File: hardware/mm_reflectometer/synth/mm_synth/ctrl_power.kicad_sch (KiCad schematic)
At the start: 64 parts, among them J1501 Screw_Terminal_01x02, J1502 Conn_01x02_Female, Q1501 FDS6890A, U1501 LTM4622A, U1502 LTC4365DDB, U1503 LM3880MF-1AF, U1504 TLV70025_WSON6, U1505 TLV62569DRL, U1506 TLV62569DRL, U1507 TLV70018_WSON6

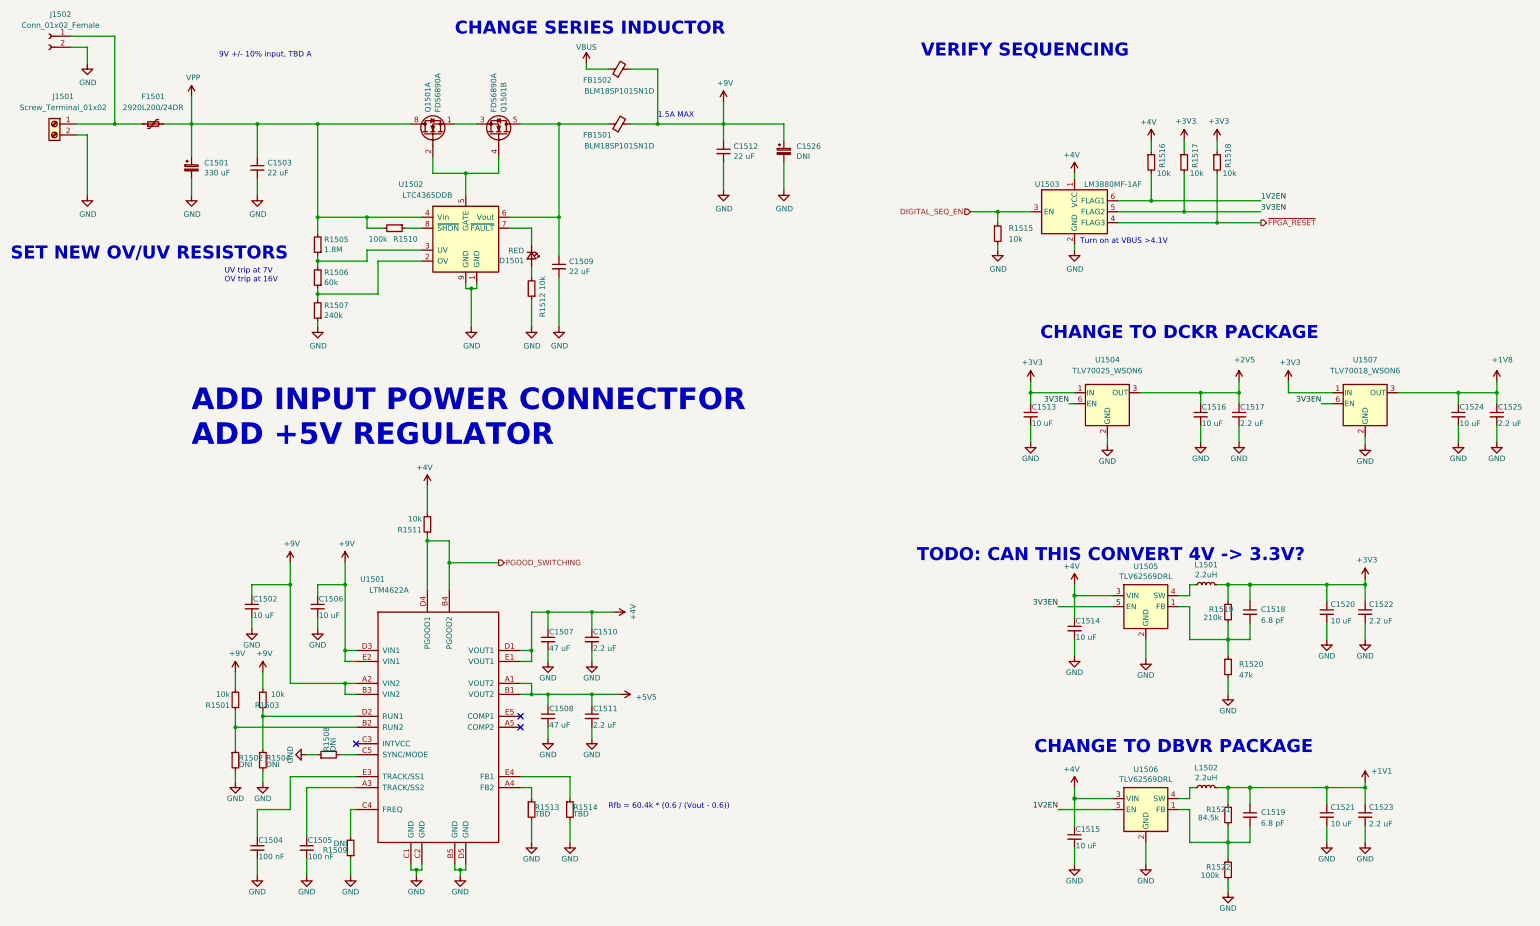
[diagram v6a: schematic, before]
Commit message: created HUSB238 eval board, added clock splitter to mm synth
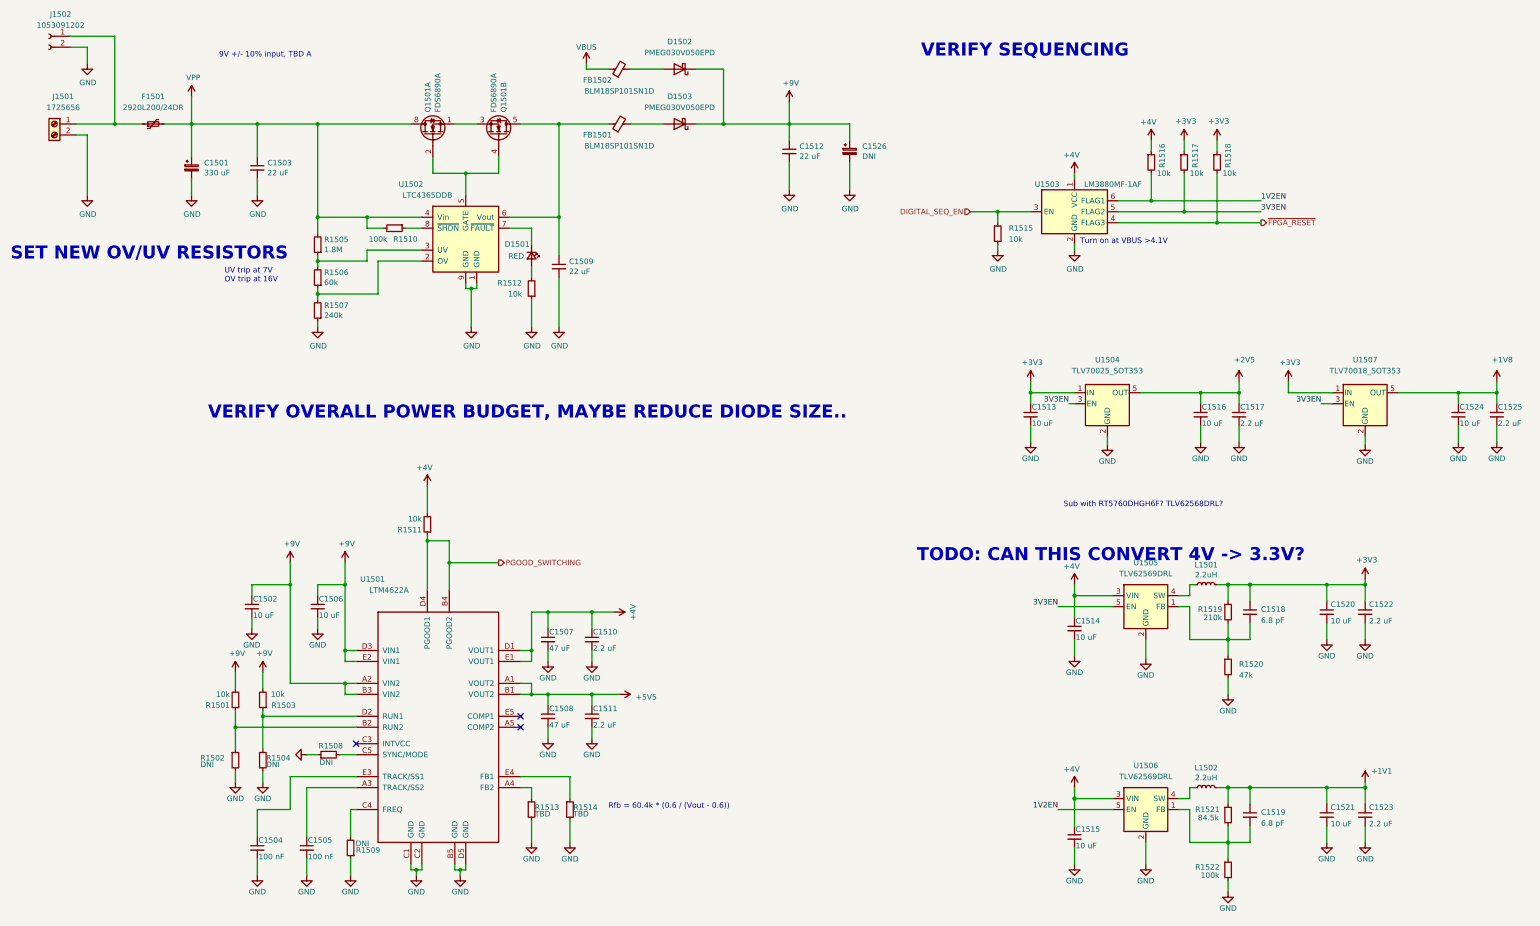
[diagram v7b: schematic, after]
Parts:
- removed U1504: TLV70025_WSON6, Package_SON:WSON-6_1.5x1.5mm_P0.5mm, symbol Regulator_Linear:TLV70025_WSON6
- removed U1507: TLV70018_WSON6, Package_SON:WSON-6_1.5x1.5mm_P0.5mm, symbol Regulator_Linear:TLV70018_WSON6
- added D1502, D1503: PMEG030V050EPD, Package_TO_SOT_SMD:Nexperia_CFP15_SOT-1289, symbol Diode:PMEG030V050EPD
- added U1504: TLV70025_SOT353, Package_TO_SOT_SMD:SOT-353_SC-70-5, symbol Regulator_Linear:TLV70025_SOT353
- added U1507: TLV70018_SOT353, Package_TO_SOT_SMD:SOT-353_SC-70-5, symbol Regulator_Linear:TLV70018_SOT353
- J1501: value Screw_Terminal_01x02 -> 1725656
- J1502: value Conn_01x02_Female -> 1053091202
- U1505, U1506: footprint Package_TO_SOT_SMD:SOT-666 -> Package_TO_SOT_SMD:SOT-563; Mfg Texas Instruments -> (none); PN TLV62569DRLR -> (none)
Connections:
- net +1V8: now also U1507.5 (OUT)
- net +2V5: now also U1504.5 (OUT)
- net +3V3: now also U1504.1 (IN), U1507.1 (IN)
- net +9V: now also D1502.3 (K), D1503.3 (K); no longer FB1501.2, FB1502.2
- net 3V3EN: now also U1504.3 (EN), U1507.3 (EN)
- net GND: now also U1504.2 (GND), U1507.2 (GND)
- new net: D1503.1 (A), D1503.2 (A), FB1501.2
- new net: D1502.1 (A), D1502.2 (A), FB1502.2
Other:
- note added: "Sub with RT5760DHGH6F? TLV62568DRL?"
- note added: "VERIFY OVERALL POWER BUDGET, MAYBE REDUCE DIODE SIZE.."
- note removed: "1.5A MAX"
- note removed: "ADD INPUT POWER CONNECTFOR ADD +5V REGULATOR"
- note removed: "CHANGE SERIES INDUCTOR"
- note removed: "CHANGE TO DBVR PACKAGE"
- note removed: "CHANGE TO DCKR PACKAGE"
- moved on the sheet: C1512, C1526

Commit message: reviewed capacitors for voltage rating and availability..
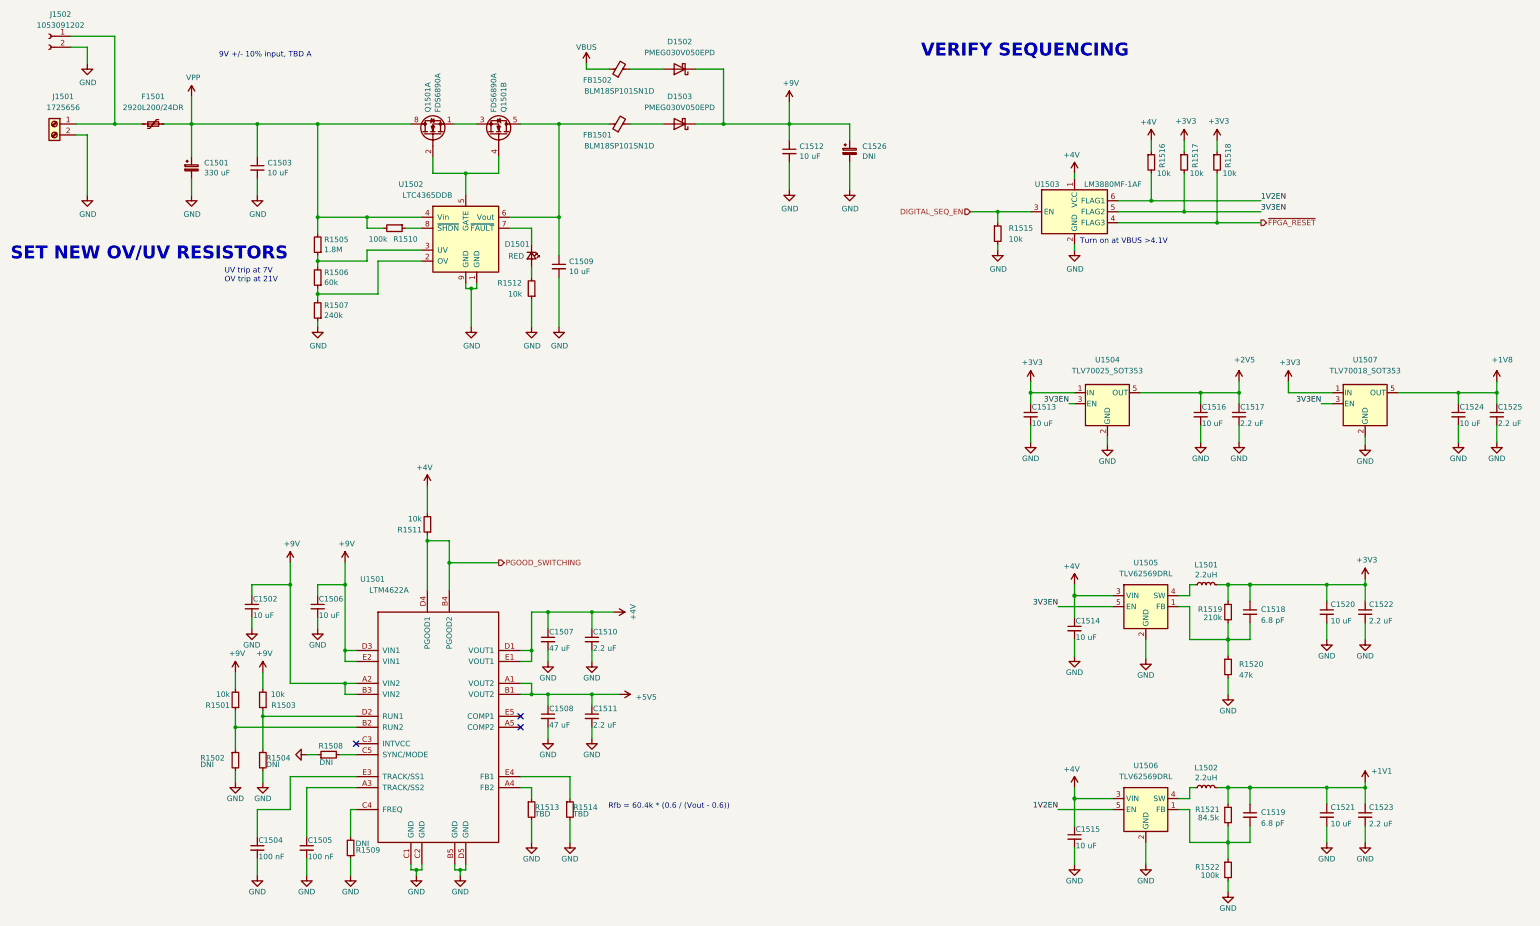
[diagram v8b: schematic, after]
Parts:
- C1501, C1526: footprint Capacitor_SMD:CP_Elec_6.3x5.9 -> Capacitor_SMD:CP_Elec_10x12.5; DIST_NAME Digi-Key -> Mouser; DIST_PN P16611CT-ND -> 80-A768MS477M1ELAE17; MAN_NAME Panasonic -> (none); MAN_PN 6SVPC330M -> (none)
- C1502, C1506: footprint Capacitor_SMD:C_0603_1608Metric -> Capacitor_SMD:C_0805_2012Metric
- C1503, C1509, C1512: value 22 uF -> 10 uF
- C1507, C1508: footprint Capacitor_SMD:C_1210_3225Metric -> Capacitor_Tantalum_SMD:CP_EIA-3528-15_AVX-H; DIST_PN 399-5514-1-ND -> (none); MAN_NAME (none) -> AVX; MAN_PN (none) -> TCNT476M016R0200A
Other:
- note added: "UV trip at 7V OV trip at 21V"
- note removed: "Sub with RT5760DHGH6F? TLV62568DRL?"
- note removed: "TODO: CAN THIS CONVERT 4V -> 3.3V?"
- note removed: "UV trip at 7V OV trip at 16V"
- note removed: "VERIFY OVERALL POWER BUDGET, MAYBE REDUCE DIODE SIZE.."
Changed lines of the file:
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@@
-    (effects (font (size 3 3) (thickness 0.6) bold) (justify left bottom))
-  )
-  (text "VERIFY OVERALL POWER BUDGET, MAYBE REDUCE DIODE SIZE.."
-    (at 77.47 110.49 0)
     (effects (font (size 3 3) (thickness 0.6) bold) (justify left bottom))
   )
@@
     (effects (font (size 1.27 1.27)) (justify left bottom))
   )
-  (text "UV trip at 7V\nOV trip at 16V" (at 81.28 78.74 0)
+  (text "UV trip at 7V\nOV trip at 21V" (at 81.28 78.74 0)
     (effects (font (size 1.27 1.27)) (justify left bottom))
   )
@@
     (effects (font (size 3 3) (thickness 0.6) bold) (justify left bottom))
   )
-  (text "Sub with RT5760DHGH6F? TLV62568DRL?\n" (at 275.59 130.81 0)
-    (effects (font (size 1.27 1.27)) (justify left bottom))
-  )
   (text "Turn on at VBUS >4.1V" (at 279.4 69.85 0)
     (effects (font (size 1.27 1.27)) (justify left bottom))
-  )
-  (text "TODO: CAN THIS CONVERT 4V -> 3.3V?" (at 331.47 143.51 180)
-    (effects (font (size 3 3) (thickness 0.6) bold) (justify right bottom))
   )
   (label "3V3EN" (at 274.32 153.67 180)
@@
       (effects (font (size 1.27 1.27)) (justify left))
     )
-    (property "Footprint" "Capacitor_SMD:CP_Elec_6.3x5.9" (id 2) (at 73.66 52.07 0)
+    (property "Footprint" "Capacitor_SMD:CP_Elec_10x12.5" (id 2) (at 73.66 52.07 0)
       (effects (font (size 1.27 1.27)) hide)
     )
@@
       (effects (font (size 1.27 1.27)) hide)
     )
-    (property "MAN_NAME" "Panasonic" (id 4) (at 73.66 52.07 0)
-      (effects (font (size 1.27 1.27)) hide)
-    )
-    (property "MAN_PN" "6SVPC330M" (id 5) (at 73.66 52.07 0)
-      (effects (font (size 1.27 1.27)) hide)
-    )
-    (property "DIST_NAME" "Digi-Key" (id 6) (at 73.66 52.07 0)
-      (effects (font (size 1.27 1.27)) hide)
-    )
-    (property "DIST_PN" "P16611CT-ND" (id 7) (at 73.66 52.07 0)
+    (property "MAN_NAME" "" (id 4) (at 73.66 52.07 0)
+      (effects (font (size 1.27 1.27)) hide)
+    )
+    (property "MAN_PN" "" (id 5) (at 73.66 52.07 0)
+      (effects (font (size 1.27 1.27)) hide)
+    )
+    (property "DIST_NAME" "Mouser" (id 6) (at 73.66 52.07 0)
+      (effects (font (size 1.27 1.27)) hide)
+    )
+    (property "DIST_PN" "80-A768MS477M1ELAE17 " (id 7) (at 73.66 52.07 0)
       (effects (font (size 1.27 1.27)) hide)
     )
@@
       (effects (font (size 1.27 1.27)) (justify left))
     )
-    (property "Footprint" "Capacitor_SMD:CP_Elec_6.3x5.9" (id 2) (at 226.06 48.26 0)
+    (property "Footprint" "Capacitor_SMD:CP_Elec_10x12.5" (id 2) (at 226.06 48.26 0)
       (effects (font (size 1.27 1.27)) hide)
     )
@@
       (effects (font (size 1.27 1.27)) hide)
     )
-    (property "MAN_NAME" "Panasonic" (id 4) (at 226.06 48.26 0)
-      (effects (font (size 1.27 1.27)) hide)
-    )
-    (property "MAN_PN" "6SVPC330M" (id 5) (at 226.06 48.26 0)
-      (effects (font (size 1.27 1.27)) hide)
-    )
-    (property "DIST_NAME" "Digi-Key" (id 6) (at 226.06 48.26 0)
-      (effects (font (size 1.27 1.27)) hide)
-    )
-    (property "DIST_PN" "P16611CT-ND" (id 7) (at 226.06 48.26 0)
+    (property "MAN_NAME" "" (id 4) (at 226.06 48.26 0)
+      (effects (font (size 1.27 1.27)) hide)
+    )
+    (property "MAN_PN" "" (id 5) (at 226.06 48.26 0)
+      (effects (font (size 1.27 1.27)) hide)
+    )
+    (property "DIST_NAME" "Mouser" (id 6) (at 226.06 48.26 0)
+      (effects (font (size 1.27 1.27)) hide)
+    )
+    (property "DIST_PN" "80-A768MS477M1ELAE17 " (id 7) (at 226.06 48.26 0)
       (effects (font (size 1.27 1.27)) hide)
     )
@@
       (effects (font (size 1.27 1.27)) (justify left))
     )
-    (property "Footprint" "Capacitor_SMD:C_0603_1608Metric" (id 2) (at 87.63 153.67 0)
+    (property "Footprint" "Capacitor_SMD:C_0805_2012Metric" (id 2) (at 87.63 153.67 0)
       (effects (font (size 1.27 1.27)) hide)
     )
@@
       (effects (font (size 1.27 1.27)) (justify left))
     )
-    (property "Value" "22 uF" (id 1) (at 91.2368 53.213 0)
+    (property "Value" "10 uF" (id 1) (at 91.2368 53.213 0)
       (effects (font (size 1.27 1.27)) (justify left))
     )
@@
       (effects (font (size 1.27 1.27)) (justify left))
     )
-    (property "Footprint" "Capacitor_SMD:C_0603_1608Metric" (id 2) (at 102.87 153.67 0)
+    (property "Footprint" "Capacitor_SMD:C_0805_2012Metric" (id 2) (at 102.87 153.67 0)
       (effects (font (size 1.27 1.27)) hide)
     )
@@
       (effects (font (size 1.27 1.27)) (justify left))
     )
-    (property "Footprint" "Capacitor_SMD:C_1210_3225Metric" (id 2) (at 156.21 161.29 0)
+    (property "Footprint" "Capacitor_Tantalum_SMD:CP_EIA-3528-15_AVX-H" (id 2) (at 156.21 161.29 0)
       (effects (font (size 1.27 1.27)) hide)
     )
@@
       (effects (font (size 1.27 1.27)) hide)
     )
-    (property "DIST_PN" "399-5514-1-ND" (id 4) (at 156.21 161.29 0)
+    (property "DIST_PN" "" (id 4) (at 156.21 161.29 0)
+      (effects (font (size 1.27 1.27)) hide)
+    )
+    (property "MAN_NAME" "AVX" (id 5) (at 156.21 161.29 0)
+      (effects (font (size 1.27 1.27)) hide)
+    )
+    (property "MAN_PN" "TCNT476M016R0200A" (id 6) (at 156.21 161.29 0)
       (effects (font (size 1.27 1.27)) hide)
     )
@@
       (effects (font (size 1.27 1.27)) (justify left))
     )
-    (property "Footprint" "Capacitor_SMD:C_1210_3225Metric" (id 2) (at 156.21 179.07 0)
+    (property "Footprint" "Capacitor_Tantalum_SMD:CP_EIA-3528-15_AVX-H" (id 2) (at 156.21 179.07 0)
       (effects (font (size 1.27 1.27)) hide)
     )
@@
       (effects (font (size 1.27 1.27)) hide)
     )
-    (property "DIST_PN" "399-5514-1-ND" (id 4) (at 156.21 179.07 0)
+    (property "DIST_PN" "" (id 4) (at 156.21 179.07 0)
+      (effects (font (size 1.27 1.27)) hide)
+    )
+    (property "MAN_NAME" "AVX" (id 5) (at 156.21 179.07 0)
+      (effects (font (size 1.27 1.27)) hide)
+    )
+    (property "MAN_PN" "TCNT476M016R0200A" (id 6) (at 156.21 179.07 0)
       (effects (font (size 1.27 1.27)) hide)
     )
@@
       (effects (font (size 1.27 1.27)) (justify left))
     )
-    (property "Value" "22 uF" (id 1) (at 161.0868 76.073 0)
+    (property "Value" "10 uF" (id 1) (at 161.0868 76.073 0)
       (effects (font (size 1.27 1.27)) (justify left))
     )
@@
       (effects (font (size 1.27 1.27)) (justify left))
     )
-    (property "Value" "22 uF" (id 1) (at 214.4268 49.403 0)
-      (effects (font (size 1.27 1.27)) (justify left))
-    )
+    (property "Value" "10 uF" (id 1) (at 214.4268 49.403 0)
+      (effects (font (size 1.27 1.27)) (justify left))
+    )
